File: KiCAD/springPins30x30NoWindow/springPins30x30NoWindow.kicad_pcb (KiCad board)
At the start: 2 copper layers, 30 x 30 mm, 24 parts, among them J1 CONN_01X03, J2 CONN_01X03, J3 CONN_01X03, J4 CONN_01X03, J5 CONN_01X03, J6 CONN_01X03, J7 CONN_01X03, J8 CONN_01X03

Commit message: nowindow pin boards done
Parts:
- removed J3, J4, J5, J6, J7, J8: CONN_01X03, myParts:M50-3130342
- removed TP1, TP13, TP14, TP2: TEST, myParts:S25-022+P25-4023
- added R1: 200k, Resistors_SMD:R_0805_HandSoldering, B.Cu at (-5.35, 10.0)
- added TP17: TEST, myParts:S25-022+P25-4023, F.Cu at (13.3, -1.27)
- added TP18: TEST, myParts:S25-022+P25-4023, F.Cu at (13.3, 1.27)
- added TP19: TEST, myParts:S25-022+P25-4023, F.Cu at (13.3, 3.81)
- added TP20: TEST, myParts:S25-022+P25-4023, F.Cu at (13.3, 6.35)
- J1, J2: value CONN_01X03 -> CONN_02X06; footprint myParts:M50-3130342 -> Pin_Headers:Pin_Header_Straight_2x06_Pitch2.54mm; moved to B.Cu
- moved TP7 41.8 mm to (-13.3, 3.81)
- moved TP5 36.4 mm to (-13.3, -1.27)
- moved J1 34.6 mm to (-6.35, 6.35)
- moved J2 31.4 mm to (3.81, 6.35)
- moved TP3 30.9 mm to (-13.3, -6.35)
- moved TP8 28.3 mm to (-13.3, 6.35)
- moved TP6 24.7 mm to (-13.3, 1.27)
- moved TP10 23.2 mm to (-1.27, 13.3)
- moved TP12 23.2 mm to (1.27, 13.3)
- moved TP11 22.9 mm to (1.27, -13.3)
- moved TP9 22.9 mm to (-1.27, -13.3)
- moved TP4 22.1 mm to (-13.3, -3.81)
- moved TP15 17.7 mm to (13.3, -6.35)
- moved TP16 17.7 mm to (13.3, -3.81)
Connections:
- net /MOSI renamed BCu
- J1 pad 1: 0_V -> /I2
- J1 pad 2: 2_V -> /RH
- J1 pad 3: /MISO -> /V2
- J2 pad 1: 0_I -> FCu
- J2 pad 2: 2_I -> /I1
- TP10 pad 1: 3_V -> /IB
- TP11 pad 1: 4_V -> /VT
- TP12 pad 1: 5_I -> /VB
- TP15 pad 1: R_V -> /V5
- TP16 pad 1: R_I -> /I5
- TP3 pad 1: 0_V -> /V6
- TP4 pad 1: 1_I -> /I6
- TP5 pad 1: 0_I -> /V4
- TP6 pad 1: 1_V -> /I4
- TP7 pad 1: 2_V -> /V2
- TP8 pad 1: 3_I -> /I2
- TP9 pad 1: 2_I -> /IT
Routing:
- net L_V: track 20.6 -> 0.00 mm, vias 2 -> 0
- net R_V: track 19.6 -> 0.00 mm, vias 2 -> 0
- net /VT: track 0.00 -> 17.5 mm
- net /IB: track 0.00 -> 17.5 mm
- net L_I: track 16.5 -> 0.00 mm, vias 1 -> 0
- net R_I: track 16.2 -> 0.00 mm, vias 1 -> 0
- net 2_I: track 16.1 -> 0.00 mm
- net 3_I: track 16.0 -> 0.00 mm
- net 3_V: track 14.0 -> 0.00 mm, vias 2 -> 0
- net /VB: track 0.00 -> 13.8 mm
- net 2_V: track 13.8 -> 0.00 mm, vias 2 -> 0
- net /IT: track 0.00 -> 13.1 mm
- net 5_I: track 12.3 -> 0.00 mm, vias 1 -> 0
- net 0_I: track 11.5 -> 0.00 mm, vias 1 -> 0
- net 4_I: track 11.0 -> 0.00 mm
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- added copper zone on B.Cu, net BCu
- added copper zone on F.Cu, net FCu
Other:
- outline, holes or cut-outs redrawn
- board text added: "+"
- board text added: "1I"
- board text added: "1V"
- board text added: "2I"
- board text added: "2V"
- board text added: "3I"
- board text added: "3V"
- board text added: "4I"
- board text added: "4V"
- board text added: "5I"
- board text added: "5V"
- board text added: "6"
- board text added: "6I"
- board text added: "6V"
- board text added: "7I"
- board text added: "7V"
- board text added: "8I"
- board text added: "8V"
- board text added: "B"
- board text added: "BCu"
- board text added: "BI"
- board text added: "BV"
- board text added: "FCu"
- board text added: "RH"
- board text added: "RL"
- board text added: "T"
- board text added: "TI"
- board text added: "TV"
- board text added: "°"
- board text removed: "0"
- board text removed: "L"
- board text removed: "R"

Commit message: update silk
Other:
- board text added: "e90ef44"
- board text removed: "efbba54"
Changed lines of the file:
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@@
   (general
     (links 18)
-    (no_connects 12)
-    (area -15.075001 -15.075001 15.075001 15.075001)
+    (no_connects 0)
+    (area -15.178476 -15.075001 15.321334 16.141)
     (thickness 1.6)
     (drawings 72)
@@
   )
   (setup
-    (last_trace_width 0.56)
+    (last_trace_width 0.25)
     (user_trace_width 0.2)
     (user_trace_width 0.56)
@@
     (effects (font (size 1 1) (thickness 0.25)) (justify mirror))
   )
-  (gr_text efbba54 (at 6.5 -12.5) (layer B.SilkS)
+  (gr_text e90ef44 (at 6.5 -12.5) (layer B.SilkS)
     (effects (font (size 0.7 0.7) (thickness 0.175)) (justify mirror))
   )
@@
     (effects (font (size 1 1) (thickness 0.25)))
   )
-  (gr_text efbba54 (at 6.5 -12.5) (layer F.SilkS)
+  (gr_text e90ef44 (at 6.5 -12.5) (layer F.SilkS)
     (effects (font (size 0.7 0.7) (thickness 0.175)))
   )

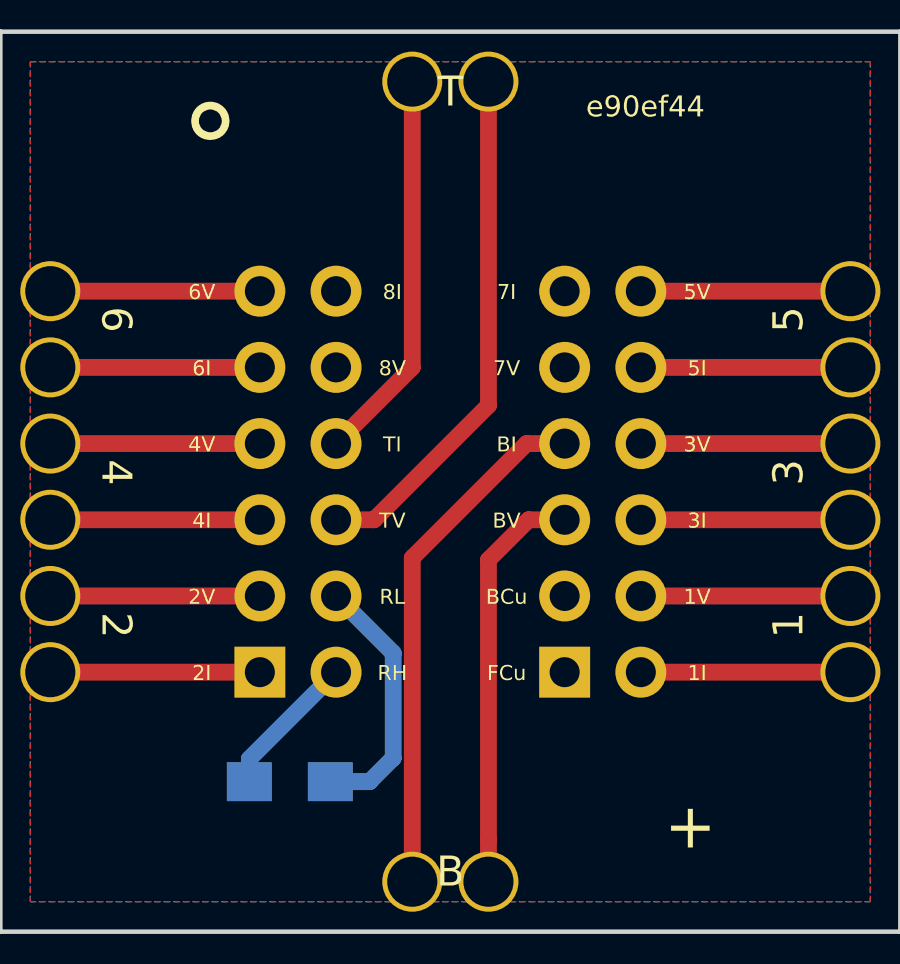
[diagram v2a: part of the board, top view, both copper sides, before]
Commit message: 30x30NoWindow spruce up
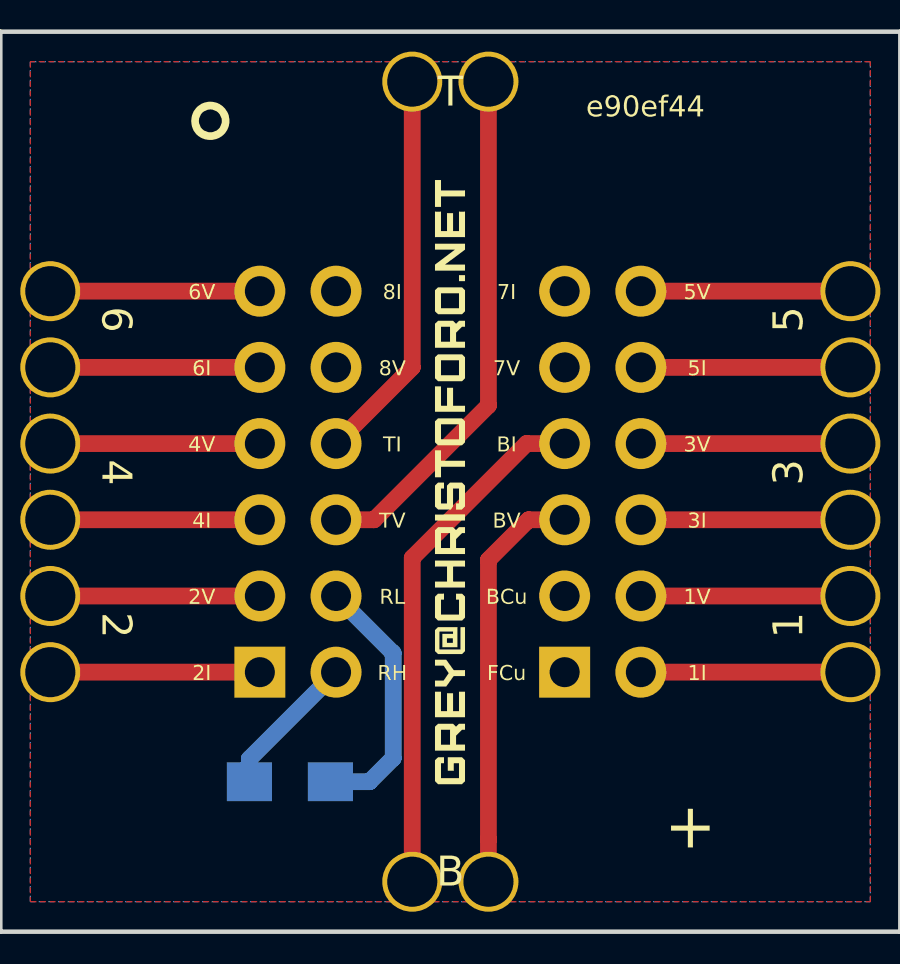
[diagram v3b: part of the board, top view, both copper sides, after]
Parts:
- added L1: GREY@CHRISTOFORO.NET, myParts:logo_small, B.Cu at (0.00, 0.00)
- added L1: GREY@CHRISTOFORO.NET, myParts:logo_small, F.Cu at (0.00, 0.00)

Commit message: update silk and generate 30x30NoWindow order.zip
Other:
- board text added: "1773e34"
- board text removed: "e90ef44"
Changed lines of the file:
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@@
     (effects (font (size 1 1) (thickness 0.25)))
   )
-  (gr_text e90ef44 (at 6.5 -12.5) (layer F.SilkS)
+  (gr_text 1773e34 (at 6.5 -12.5) (layer F.SilkS)
     (effects (font (size 0.7 0.7) (thickness 0.175)))
   )

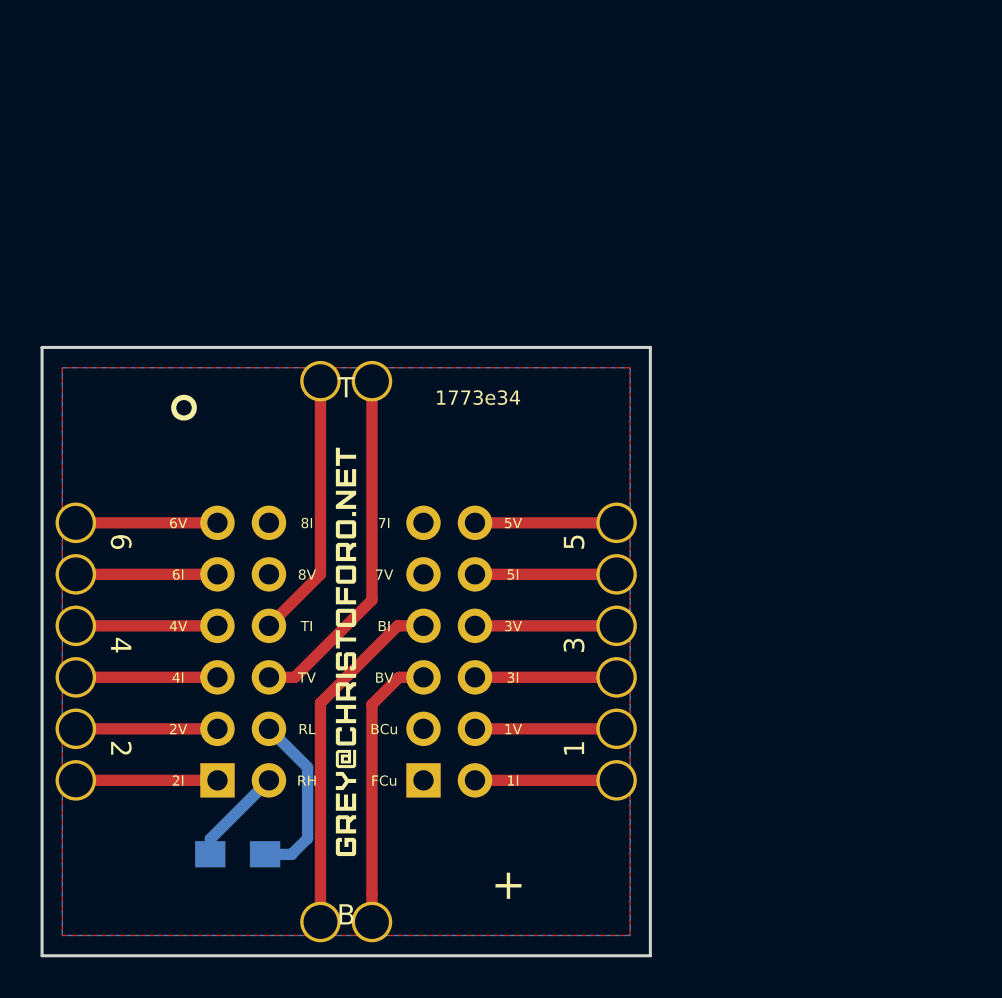
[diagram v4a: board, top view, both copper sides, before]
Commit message: fixed up newMux so that parts don't collide
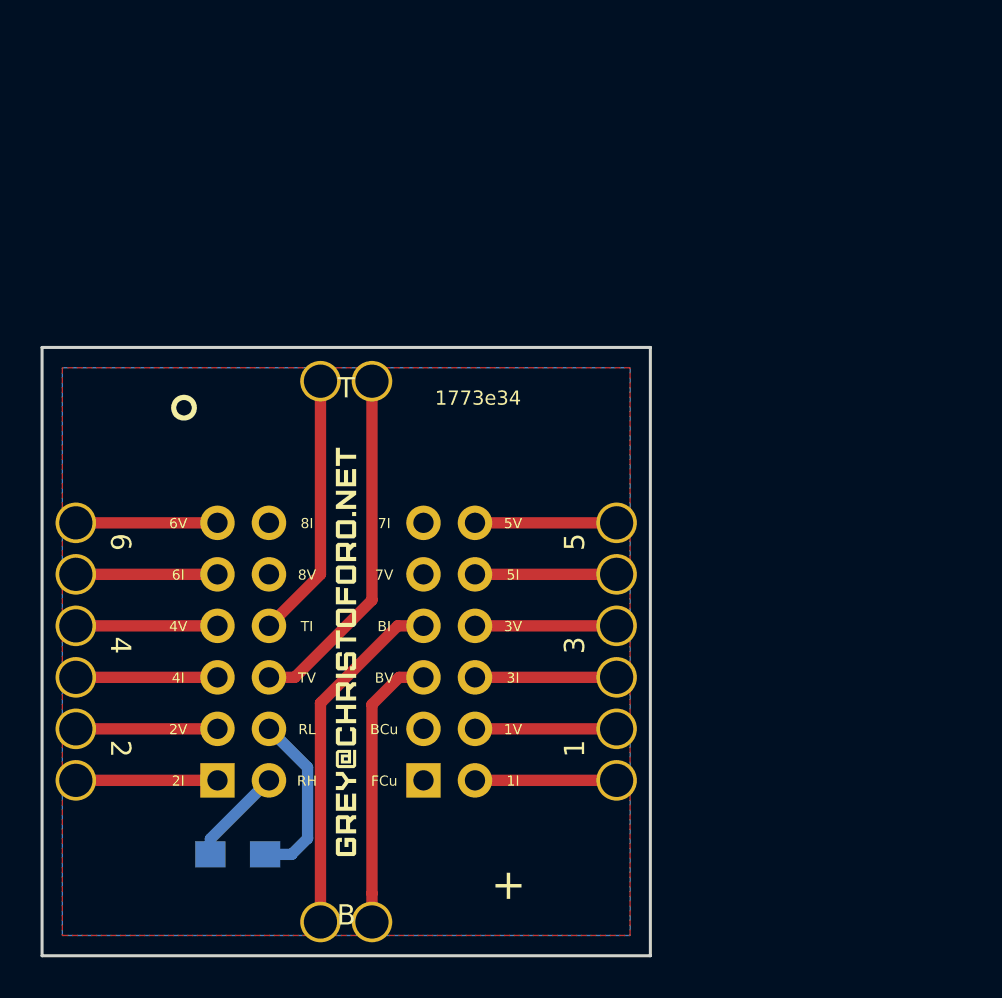
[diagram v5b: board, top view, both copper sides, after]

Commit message: update silk
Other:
- board text added: "1ad7c5f"
- board text removed: "1773e34"
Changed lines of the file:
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@@
     (effects (font (size 1 1) (thickness 0.25)))
   )
-  (gr_text 1773e34 (at 6.5 -12.5) (layer F.SilkS)
+  (gr_text 1ad7c5f (at 6.5 -12.5) (layer F.SilkS)
     (effects (font (size 0.7 0.7) (thickness 0.175)))
   )

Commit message: make spring pin board pin holders smaller, update base1x, update mux design controller board
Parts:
- added JP1: Jumper_NO_Small, Connectors:GS2, B.Cu at (3.81, 10.0)
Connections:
- J1 pad 10: (no net) -> Net-(J1-Pad10)
- J1 pad 12: (no net) -> Net-(J1-Pad12)
- J2 pad 1: FCu -> /FCu
- J2 pad 11: (no net) -> Net-(J2-Pad11)
- J2 pad 3: BCu -> /BCu
- J2 pad 9: (no net) -> Net-(J2-Pad9)
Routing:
- net /FCu: track 0.00 -> 3.04 mm
- added copper zone on B.Cu, net /BCu
- added copper zone on F.Cu, net /FCu
- removed copper zone on B.Cu, net BCu
- removed copper zone on F.Cu, net FCu

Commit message: update silk
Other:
- board text added: "c75b306"
- board text removed: "1ad7c5f"
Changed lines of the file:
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@@
       (effects (font (size 1 1) (thickness 0.15)) (justify mirror))
     )
-    (fp_text value CONN_02X06 (at 1.27 -15.03) (layer B.Fab)
+    (fp_text value CONN_02X06 (at 1.27 -15.03) (layer B.Fab) hide
       (effects (font (size 1 1) (thickness 0.15)) (justify mirror))
     )
@@
       (effects (font (size 1 1) (thickness 0.15)) (justify mirror))
     )
-    (fp_text value CONN_02X06 (at 1.27 -15.03) (layer B.Fab)
+    (fp_text value CONN_02X06 (at 1.27 -15.03) (layer B.Fab) hide
       (effects (font (size 1 1) (thickness 0.15)) (justify mirror))
     )
@@
     (effects (font (size 1 1) (thickness 0.25)))
   )
-  (gr_text 1ad7c5f (at 6.5 -12.5) (layer F.SilkS)
+  (gr_text c75b306 (at 6.5 -12.5) (layer F.SilkS)
     (effects (font (size 0.7 0.7) (thickness 0.175)))
   )
